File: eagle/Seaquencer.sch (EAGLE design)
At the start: 41 parts, among them IC1 ATMEGA48/88/168, IC2 74HC595N

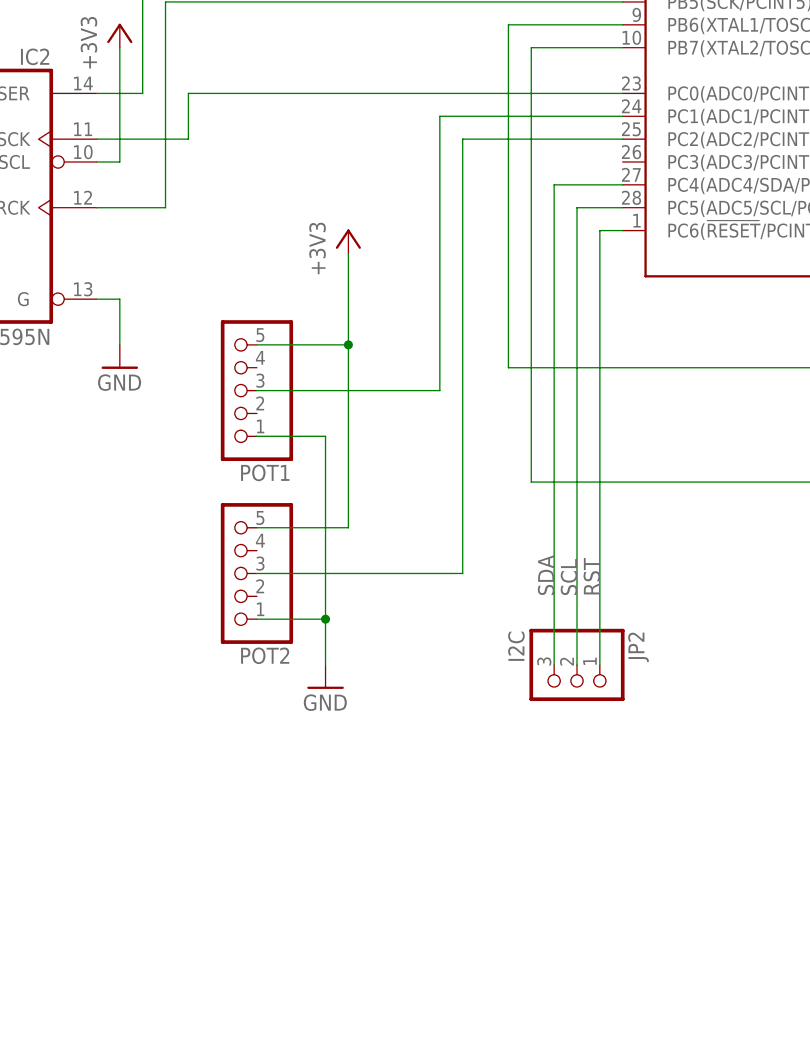
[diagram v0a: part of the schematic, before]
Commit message: Sequencer.brd: Add LED for Rotary Encdoer
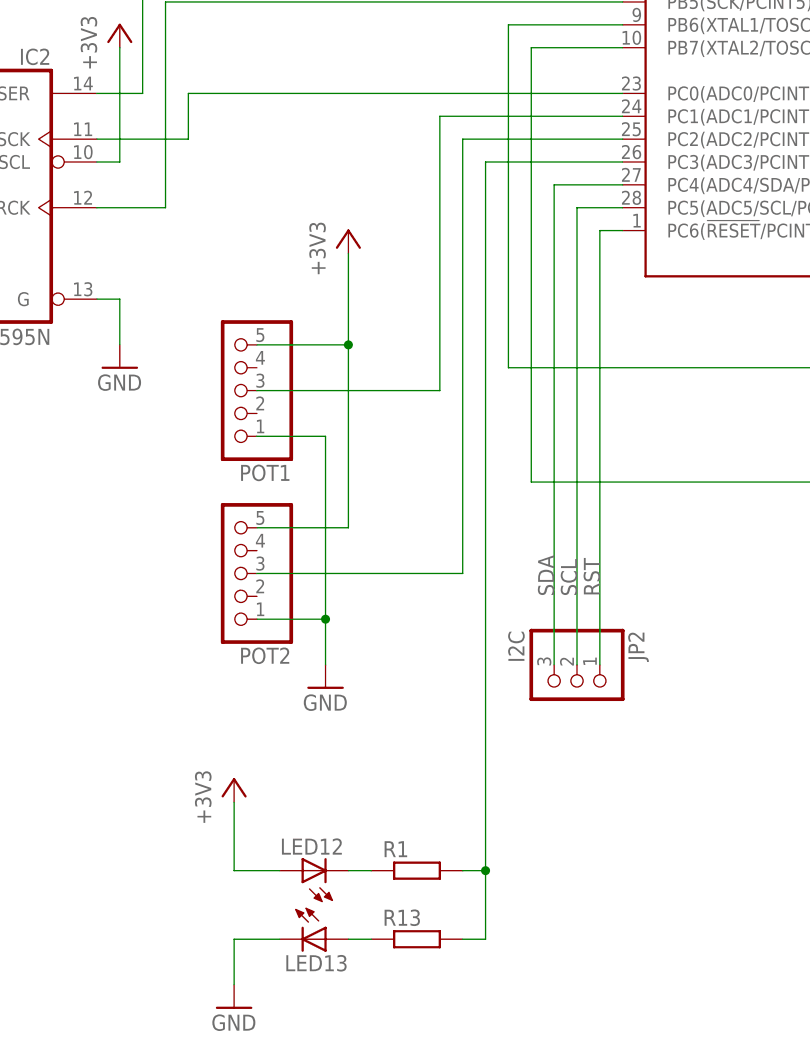
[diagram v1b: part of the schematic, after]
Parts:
- added LED12, LED13: (no value), led:LED3MM
- added R1, R13: (no value), rcl:R-EU_0207/7
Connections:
- new net N$14: IC1.PC3(ADC3/PCINT11), R1.2, R13.2
- new net N$32: LED12.C, R1.1
- new net N$37: LED13.A, R13.1
- net +3V3: now also LED12.A
- net GND: now also LED13.C
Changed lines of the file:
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@@
 <part name="POT1" library="pinhead" deviceset="PINHD-1X5" device=""/>
 <part name="POT2" library="pinhead" deviceset="PINHD-1X5" device=""/>
+<part name="LED12" library="led" deviceset="LED" device="3MM"/>
+<part name="R1" library="rcl" deviceset="R-EU_" device="0207/7"/>
+<part name="LED13" library="led" deviceset="LED" device="3MM"/>
+<part name="R13" library="rcl" deviceset="R-EU_" device="0207/7"/>
+<part name="+3V6" library="supply1" deviceset="+3V3" device=""/>
+<part name="GND12" library="supply1" deviceset="GND" device=""/>
 </parts>
 <sheets>
@@
 <instance part="POT1" gate="A" x="60.96" y="33.02" rot="R180"/>
 <instance part="POT2" gate="A" x="60.96" y="12.7" rot="R180"/>
+<instance part="LED12" gate="G$1" x="68.58" y="-20.32" rot="R90"/>
+<instance part="R1" gate="G$1" x="81.28" y="-20.32"/>
+<instance part="LED13" gate="G$1" x="71.12" y="-27.94" rot="R270"/>
+<instance part="R13" gate="G$1" x="81.28" y="-27.94"/>
+<instance part="+3V6" gate="G$1" x="60.96" y="-10.16"/>
+<instance part="GND12" gate="1" x="60.96" y="-35.56"/>
 </instances>
 <busses>
@@
 <pinref part="POT2" gate="A" pin="1"/>
 </segment>
+<segment>
+<pinref part="LED13" gate="G$1" pin="C"/>
+<wire x1="66.04" y1="-27.94" x2="60.96" y2="-27.94" width="0.1524" layer="91"/>
+<wire x1="60.96" y1="-27.94" x2="60.96" y2="-33.02" width="0.1524" layer="91"/>
+<pinref part="GND12" gate="1" pin="GND"/>
+</segment>
 </net>
 <net name="+3V3" class="0">
@@
 <pinref part="POT2" gate="A" pin="5"/>
 </segment>
+<segment>
+<pinref part="LED12" gate="G$1" pin="A"/>
+<wire x1="66.04" y1="-20.32" x2="60.96" y2="-20.32" width="0.1524" layer="91"/>
+<pinref part="+3V6" gate="G$1" pin="+3V3"/>
+<wire x1="60.96" y1="-20.32" x2="60.96" y2="-12.7" width="0.1524" layer="91"/>
+</segment>
 </net>
 <net name="N$15" class="0">
@@
 </segment>
 </net>
+<net name="N$14" class="0">
+<segment>
+<pinref part="R1" gate="G$1" pin="2"/>
+<wire x1="86.36" y1="-20.32" x2="88.9" y2="-20.32" width="0.1524" layer="91"/>
+<wire x1="88.9" y1="-20.32" x2="88.9" y2="58.42" width="0.1524" layer="91"/>
+<pinref part="IC1" gate="G$1" pin="PC3(ADC3/PCINT11)"/>
+<wire x1="88.9" y1="58.42" x2="104.14" y2="58.42" width="0.1524" layer="91"/>
+<pinref part="R13" gate="G$1" pin="2"/>
+<wire x1="86.36" y1="-27.94" x2="88.9" y2="-27.94" width="0.1524" layer="91"/>
+<wire x1="88.9" y1="-27.94" x2="88.9" y2="-20.32" width="0.1524" layer="91"/>
+<junction x="88.9" y="-20.32"/>
+</segment>
+</net>
+<net name="N$32" class="0">
+<segment>
+<pinref part="R1" gate="G$1" pin="1"/>
+<pinref part="LED12" gate="G$1" pin="C"/>
+<wire x1="73.66" y1="-20.32" x2="76.2" y2="-20.32" width="0.1524" layer="91"/>
+</segment>
+</net>
+<net name="N$37" class="0">
+<segment>
+<pinref part="LED13" gate="G$1" pin="A"/>
+<pinref part="R13" gate="G$1" pin="1"/>
+<wire x1="73.66" y1="-27.94" x2="76.2" y2="-27.94" width="0.1524" layer="91"/>
+</segment>
+</net>

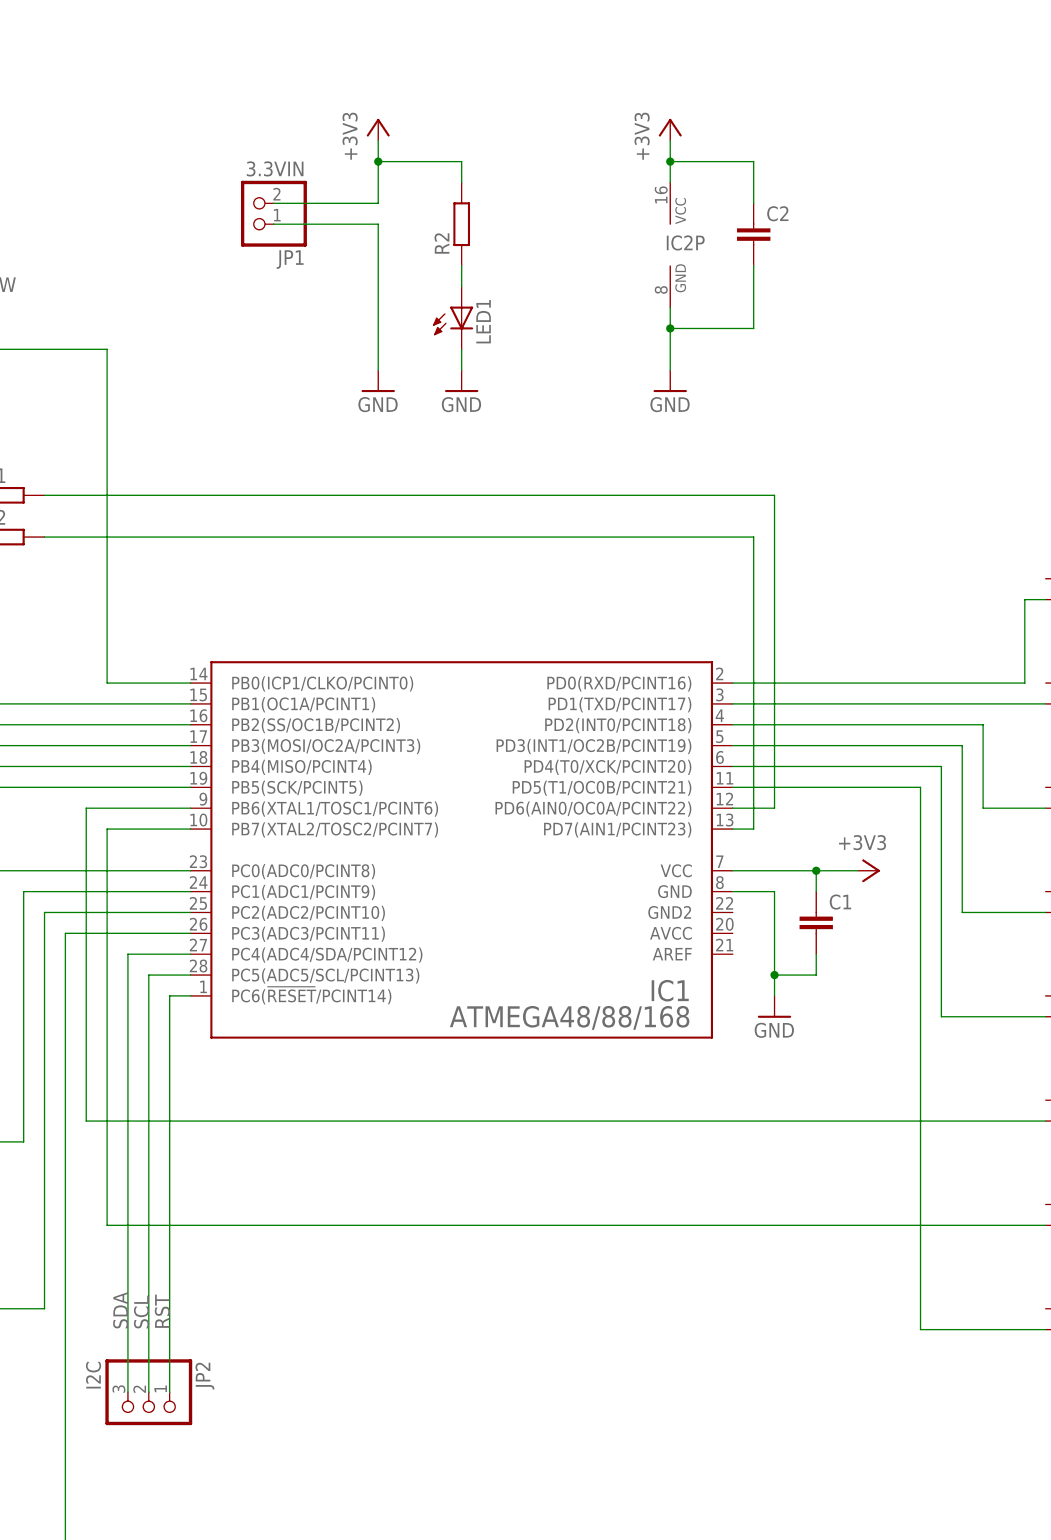
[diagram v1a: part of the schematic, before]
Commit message: Sequencer.brd: 部品再配置前
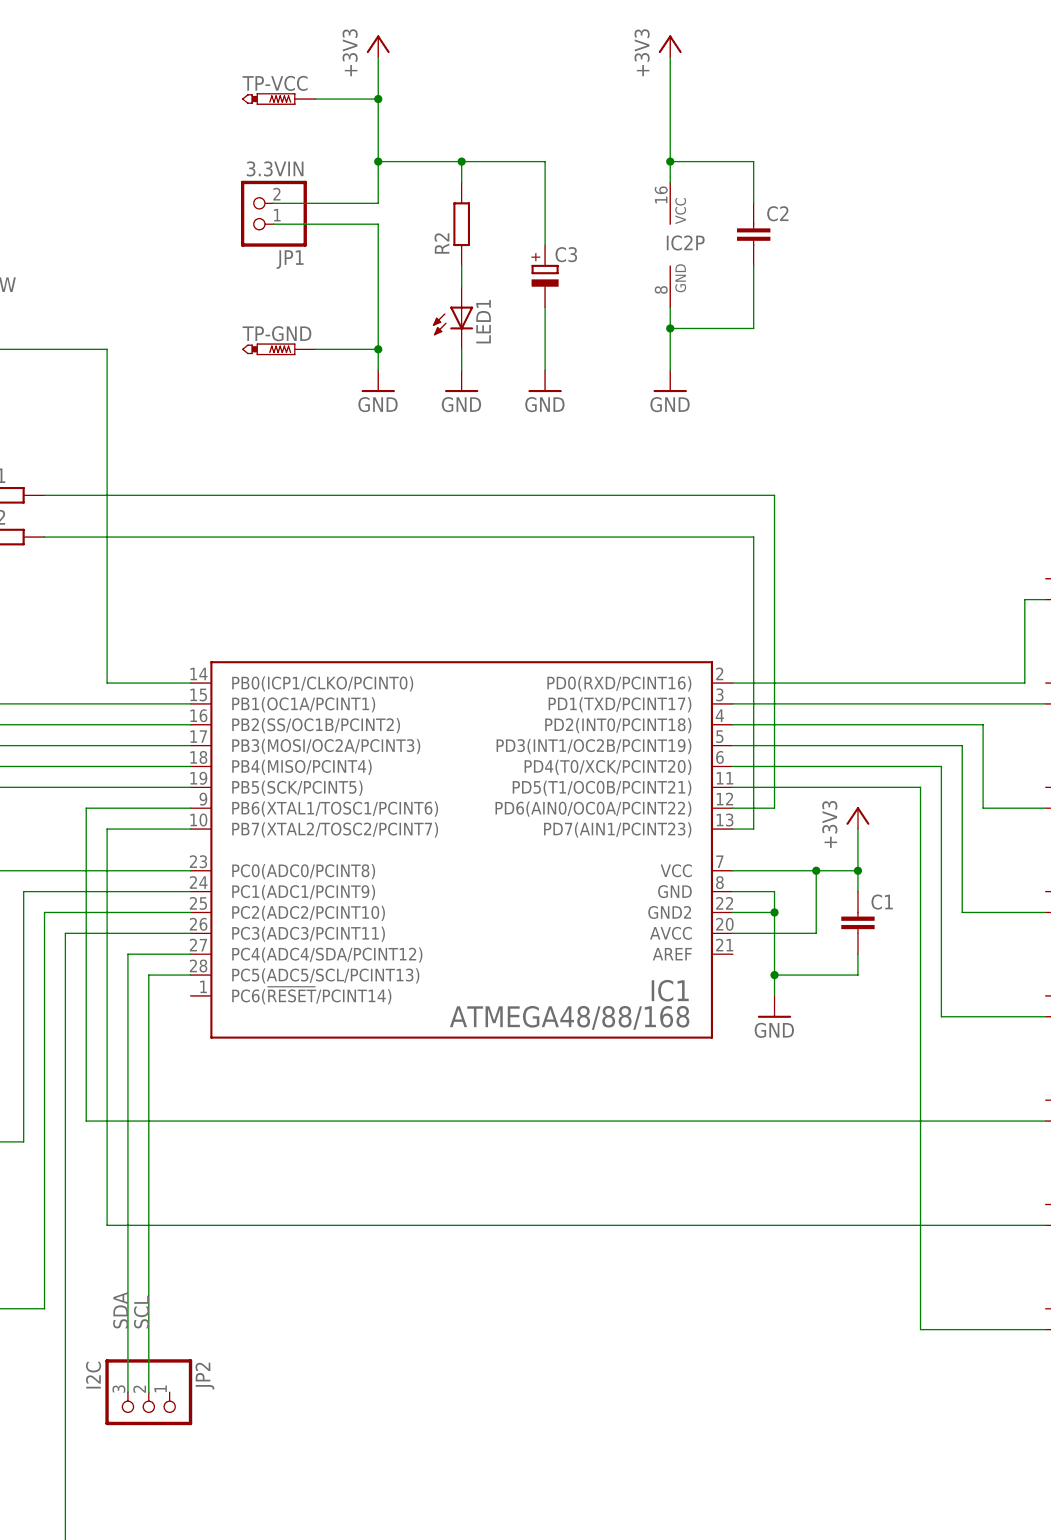
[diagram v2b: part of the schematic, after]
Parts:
- added C3: (no value), rcl:CPOL-EUE2.5-6
- added TP-GND, TP-VCC: PTR1PAD1-13, testpad:PTR1PAD1-13
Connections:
- removed net RST: IC1.PC6(!RESET!/PCINT14), JP2.1
- net +3V3: now also C3.+, IC1.AVCC, TP-VCC.TP
- net GND: now also C3.-, IC1.GND2, TP-GND.TP
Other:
- moved on the sheet: C1
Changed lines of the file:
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@@
 <setting verticaltext="up"/>
 </settings>
-<grid distance="0.1" unitdist="inch" unit="inch" style="dots" multiple="1" display="yes" altdistance="0.01" altunitdist="inch" altunit="inch"/>
+<grid distance="0.1" unitdist="inch" unit="inch" style="lines" multiple="1" display="no" altdistance="0.01" altunitdist="inch" altunit="inch"/>
 <layers>
 <layer number="1" name="Top" color="4" fill="1" visible="no" active="no"/>
@@
 <part name="+3V6" library="supply1" deviceset="+3V3" device=""/>
 <part name="GND12" library="supply1" deviceset="GND" device=""/>
+<part name="C3" library="rcl" deviceset="CPOL-EU" device="E2.5-6"/>
+<part name="GND13" library="supply1" deviceset="GND" device=""/>
+<part name="TP-GND" library="testpad" deviceset="PTR1" device="PAD1-13"/>
+<part name="TP-VCC" library="testpad" deviceset="PTR1" device="PAD1-13"/>
 </parts>
 <sheets>
@@
 <instance part="U$8" gate="G$1" x="213.36" y="12.7" rot="R270"/>
 <instance part="JP1" gate="G$1" x="111.76" y="147.32" rot="R180"/>
-<instance part="+3V1" gate="G$1" x="127" y="157.48"/>
+<instance part="+3V1" gate="G$1" x="127" y="167.64"/>
 <instance part="GND1" gate="1" x="127" y="124.46"/>
 <instance part="GND3" gate="1" x="228.6" y="5.08"/>
@@
 <instance part="GND7" gate="1" x="48.26" y="35.56"/>
 <instance part="IC2" gate="P" x="162.56" y="142.24"/>
-<instance part="+3V4" gate="G$1" x="162.56" y="157.48"/>
+<instance part="+3V4" gate="G$1" x="162.56" y="167.64"/>
 <instance part="GND8" gate="1" x="162.56" y="124.46"/>
 <instance part="C2" gate="G$1" x="172.72" y="144.78"/>
@@
 <instance part="GND10" gate="1" x="27.94" y="127"/>
 <instance part="IC1" gate="G$1" x="137.16" y="68.58"/>
-<instance part="+3V2" gate="G$1" x="187.96" y="66.04" rot="R270"/>
+<instance part="+3V2" gate="G$1" x="185.42" y="73.66"/>
 <instance part="GND2" gate="1" x="175.26" y="48.26"/>
-<instance part="C1" gate="G$1" x="180.34" y="60.96"/>
+<instance part="C1" gate="G$1" x="185.42" y="60.96"/>
 <instance part="RE_AB" gate="A" x="12.7" y="114.3" rot="R180"/>
 <instance part="RE_SW" gate="A" x="12.7" y="137.16" rot="R180"/>
@@
 <instance part="+3V6" gate="G$1" x="60.96" y="-10.16"/>
 <instance part="GND12" gate="1" x="60.96" y="-35.56"/>
+<instance part="C3" gate="G$1" x="147.32" y="139.7"/>
+<instance part="GND13" gate="1" x="147.32" y="124.46"/>
+<instance part="TP-GND" gate="G$1" x="116.84" y="129.54" rot="R270"/>
+<instance part="TP-VCC" gate="G$1" x="116.84" y="160.02" rot="R270"/>
 </instances>
 <busses>
@@
 <pinref part="GND1" gate="1" pin="GND"/>
 <wire x1="114.3" y1="144.78" x2="127" y2="144.78" width="0.1524" layer="91"/>
-<wire x1="127" y1="144.78" x2="127" y2="127" width="0.1524" layer="91"/>
+<wire x1="127" y1="144.78" x2="127" y2="129.54" width="0.1524" layer="91"/>
+<wire x1="127" y1="129.54" x2="127" y2="127" width="0.1524" layer="91"/>
+<wire x1="119.38" y1="129.54" x2="127" y2="129.54" width="0.1524" layer="91"/>
+<junction x="127" y="129.54"/>
+<pinref part="TP-GND" gate="G$1" pin="TP"/>
 </segment>
 <segment>
@@
 <pinref part="GND2" gate="1" pin="GND"/>
 <wire x1="170.18" y1="63.5" x2="175.26" y2="63.5" width="0.1524" layer="91"/>
-<wire x1="175.26" y1="63.5" x2="175.26" y2="53.34" width="0.1524" layer="91"/>
+<wire x1="175.26" y1="63.5" x2="175.26" y2="60.96" width="0.1524" layer="91"/>
 <pinref part="C1" gate="G$1" pin="2"/>
+<wire x1="175.26" y1="60.96" x2="175.26" y2="53.34" width="0.1524" layer="91"/>
 <wire x1="175.26" y1="53.34" x2="175.26" y2="50.8" width="0.1524" layer="91"/>
-<wire x1="180.34" y1="55.88" x2="180.34" y2="53.34" width="0.1524" layer="91"/>
-<wire x1="180.34" y1="53.34" x2="175.26" y2="53.34" width="0.1524" layer="91"/>
+<wire x1="185.42" y1="55.88" x2="185.42" y2="53.34" width="0.1524" layer="91"/>
+<wire x1="185.42" y1="53.34" x2="175.26" y2="53.34" width="0.1524" layer="91"/>
 <junction x="175.26" y="53.34"/>
+<pinref part="IC1" gate="G$1" pin="GND2"/>
+<wire x1="170.18" y1="60.96" x2="175.26" y2="60.96" width="0.1524" layer="91"/>
+<junction x="175.26" y="60.96"/>
 </segment>
 <segment>
@@
 <pinref part="GND12" gate="1" pin="GND"/>
 </segment>
+<segment>
+<pinref part="C3" gate="G$1" pin="-"/>
+<pinref part="GND13" gate="1" pin="GND"/>
+<wire x1="147.32" y1="134.62" x2="147.32" y2="127" width="0.1524" layer="91"/>
+</segment>
 </net>
 <net name="+3V3" class="0">
@@
 <pinref part="JP1" gate="G$1" pin="2"/>
 <pinref part="R2" gate="G$1" pin="2"/>
-<wire x1="127" y1="152.4" x2="127" y2="154.94" width="0.1524" layer="91"/>
+<wire x1="127" y1="152.4" x2="127" y2="160.02" width="0.1524" layer="91"/>
+<wire x1="127" y1="160.02" x2="127" y2="165.1" width="0.1524" layer="91"/>
 <wire x1="127" y1="152.4" x2="137.16" y2="152.4" width="0.1524" layer="91"/>
 <wire x1="137.16" y1="152.4" x2="137.16" y2="149.86" width="0.1524" layer="91"/>
 <junction x="127" y="152.4"/>
+<pinref part="C3" gate="G$1" pin="+"/>
+<wire x1="137.16" y1="152.4" x2="147.32" y2="152.4" width="0.1524" layer="91"/>
+<wire x1="147.32" y1="152.4" x2="147.32" y2="142.24" width="0.1524" layer="91"/>
+<junction x="137.16" y="152.4"/>
+<pinref part="TP-VCC" gate="G$1" pin="TP"/>
+<wire x1="119.38" y1="160.02" x2="127" y2="160.02" width="0.1524" layer="91"/>
+<junction x="127" y="160.02"/>
 </segment>
 <segment>
@@
 <pinref part="+3V4" gate="G$1" pin="+3V3"/>
 <pinref part="IC2" gate="P" pin="VCC"/>
-<wire x1="162.56" y1="154.94" x2="162.56" y2="152.4" width="0.1524" layer="91"/>
+<wire x1="162.56" y1="165.1" x2="162.56" y2="152.4" width="0.1524" layer="91"/>
 <wire x1="162.56" y1="152.4" x2="162.56" y2="149.86" width="0.1524" layer="91"/>
 <wire x1="162.56" y1="152.4" x2="172.72" y2="152.4" width="0.1524" layer="91"/>
@@
 <pinref part="C1" gate="G$1" pin="1"/>
 <wire x1="180.34" y1="66.04" x2="185.42" y2="66.04" width="0.1524" layer="91"/>
-<wire x1="180.34" y1="63.5" x2="180.34" y2="66.04" width="0.1524" layer="91"/>
+<wire x1="185.42" y1="66.04" x2="185.42" y2="71.12" width="0.1524" layer="91"/>
+<wire x1="185.42" y1="63.5" x2="185.42" y2="66.04" width="0.1524" layer="91"/>
+<junction x="185.42" y="66.04"/>
+<pinref part="IC1" gate="G$1" pin="AVCC"/>
+<wire x1="170.18" y1="58.42" x2="180.34" y2="58.42" width="0.1524" layer="91"/>
+<wire x1="180.34" y1="58.42" x2="180.34" y2="66.04" width="0.1524" layer="91"/>
 <junction x="180.34" y="66.04"/>
 </segment>
@@
 </segment>
 </net>
-<net name="RST" class="0">
-<segment>
-<pinref part="IC1" gate="G$1" pin="PC6(!RESET!/PCINT14)"/>
-<wire x1="104.14" y1="50.8" x2="101.6" y2="50.8" width="0.1524" layer="91"/>
-<pinref part="JP2" gate="A" pin="1"/>
-<wire x1="101.6" y1="50.8" x2="101.6" y2="2.54" width="0.1524" layer="91"/>
-<label x="101.6" y="10.16" size="1.778" layer="95" rot="R90"/>
-</segment>
-</net>
